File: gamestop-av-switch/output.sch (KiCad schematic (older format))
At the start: 10 parts

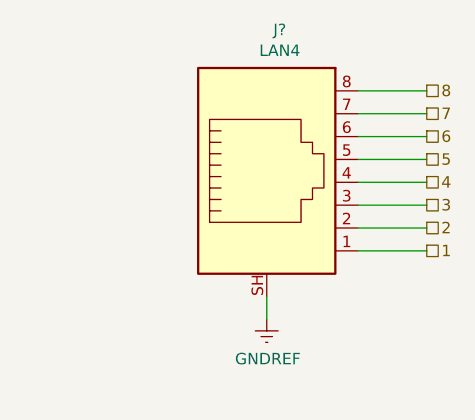
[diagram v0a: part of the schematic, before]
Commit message: Cleaning up extra ethernet pins
Setting no connects on the ports themselves and eliminating the extra
heirarchal labels and pins
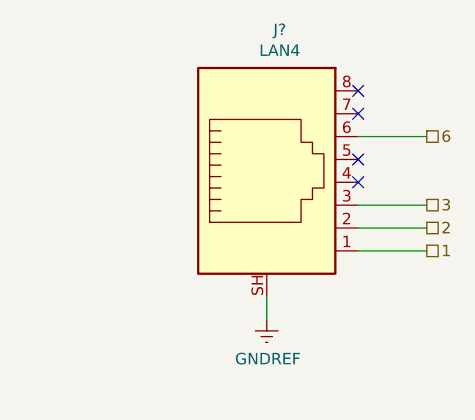
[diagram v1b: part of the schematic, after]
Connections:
- net 4: no longer names the net of J?.4
- net 5: no longer names the net of J?.5
- net 7: no longer names the net of J?.7
- net 8: no longer names the net of J?.8
- no-connect marks 0 -> 4
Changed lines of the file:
@@
 Text HLabel 9850 3600 2    50   UnSpc ~ 0
 3
-Text HLabel 9850 3500 2    50   UnSpc ~ 0
-4
-Text HLabel 9850 3400 2    50   UnSpc ~ 0
-5
 Text HLabel 9850 3300 2    50   UnSpc ~ 0
 6
-Text HLabel 9850 3200 2    50   UnSpc ~ 0
-7
-Text HLabel 9850 3100 2    50   UnSpc ~ 0
-8
-Wire Wire Line
-	9550 3100 9850 3100
-Wire Wire Line
-	9550 3200 9850 3200
 Wire Wire Line
 	9550 3300 9850 3300
-Wire Wire Line
-	9550 3400 9850 3400
-Wire Wire Line
-	9550 3500 9850 3500
 Wire Wire Line
 	9550 3600 9850 3600
@@
 Wire Wire Line
 	2000 3400 2200 3400
+NoConn ~ 9550 3100
+NoConn ~ 9550 3200
+NoConn ~ 9550 3400
+NoConn ~ 9550 3500
 $EndSCHEMATC

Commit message: Annotating and satisfying ERC
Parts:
- gave numbers to parts that had none: 10
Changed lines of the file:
@@
 AR Path="/60F422FE/60FA378A" Ref="J?"  Part="1"
 AR Path="/60F4248B/60FA378A" Ref="J?"  Part="1"
-AR Path="/60F434DB/60FA378A" Ref="J?"  Part="1"
-F 0 "J?" H 4850 3375 50  0000 L CNN
+AR Path="/60F434DB/60FA378A" Ref="J74"  Part="1"
+F 0 "J74" H 4850 3375 50  0000 L CNN
 F 1 "RD5" H 4850 3284 50  0000 L CNN
 F 2 "" H 4750 3400 50  0001 C CNN
@@
 AR Path="/60F422FE/60FA3790" Ref="J?"  Part="1"
 AR Path="/60F4248B/60FA3790" Ref="J?"  Part="1"
-AR Path="/60F434DB/60FA3790" Ref="J?"  Part="1"
-F 0 "J?" H 7150 4017 50  0000 C CNN
+AR Path="/60F434DB/60FA3790" Ref="J76"  Part="1"
+F 0 "J76" H 7150 4017 50  0000 C CNN
 F 1 "SV5" H 7150 3926 50  0000 C CNN
 F 2 "" H 7150 3650 50  0001 C CNN
@@
 AR Path="/60F422FE/60FA3796" Ref="J?"  Part="1"
 AR Path="/60F4248B/60FA3796" Ref="J?"  Part="1"
-AR Path="/60F434DB/60FA3796" Ref="J?"  Part="1"
-F 0 "J?" H 9207 4167 50  0000 C CNN
+AR Path="/60F434DB/60FA3796" Ref="J77"  Part="1"
+F 0 "J77" H 9207 4167 50  0000 C CNN
 F 1 "LAN4" H 9207 4076 50  0000 C CNN
 F 2 "" V 9150 3525 50  0001 C CNN
@@
 AR Path="/60F422FE/60FA379C" Ref="J?"  Part="1"
 AR Path="/60F4248B/60FA379C" Ref="J?"  Part="1"
-AR Path="/60F434DB/60FA379C" Ref="J?"  Part="1"
-F 0 "J?" H 4850 3825 50  0000 L CNN
+AR Path="/60F434DB/60FA379C" Ref="J75"  Part="1"
+F 0 "J75" H 4850 3825 50  0000 L CNN
 F 1 "G5" H 4850 3734 50  0000 L CNN
 F 2 "" H 4750 3850 50  0001 C CNN
@@
 AR Path="/60F422FE/60FA37A2" Ref="J?"  Part="1"
 AR Path="/60F4248B/60FA37A2" Ref="J?"  Part="1"
-AR Path="/60F434DB/60FA37A2" Ref="J?"  Part="1"
-F 0 "J?" H 3600 3375 50  0000 L CNN
+AR Path="/60F434DB/60FA37A2" Ref="J72"  Part="1"
+F 0 "J72" H 3600 3375 50  0000 L CNN
 F 1 "B5" H 3600 3284 50  0000 L CNN
 F 2 "" H 3500 3400 50  0001 C CNN
@@
 AR Path="/60F422FE/60FA37A8" Ref="J?"  Part="1"
 AR Path="/60F4248B/60FA37A8" Ref="J?"  Part="1"
-AR Path="/60F434DB/60FA37A8" Ref="J?"  Part="1"
-F 0 "J?" H 3600 3825 50  0000 L CNN
+AR Path="/60F434DB/60FA37A8" Ref="J73"  Part="1"
+F 0 "J73" H 3600 3825 50  0000 L CNN
 F 1 "Y5" H 3600 3734 50  0000 L CNN
 F 2 "" H 3500 3850 50  0001 C CNN
@@
 AR Path="/60F422FE/60FA37AE" Ref="J?"  Part="1"
 AR Path="/60F4248B/60FA37AE" Ref="J?"  Part="1"
-AR Path="/60F434DB/60FA37AE" Ref="J?"  Part="1"
-F 0 "J?" H 2500 3375 50  0000 L CNN
+AR Path="/60F434DB/60FA37AE" Ref="J70"  Part="1"
+F 0 "J70" H 2500 3375 50  0000 L CNN
 F 1 "R5-2" H 2500 3284 50  0000 L CNN
 F 2 "" H 2400 3400 50  0001 C CNN
@@
 AR Path="/60F422FE/60FA37B4" Ref="J?"  Part="1"
 AR Path="/60F4248B/60FA37B4" Ref="J?"  Part="1"
-AR Path="/60F434DB/60FA37B4" Ref="J?"  Part="1"
-F 0 "J?" H 2500 3825 50  0000 L CNN
+AR Path="/60F434DB/60FA37B4" Ref="J71"  Part="1"
+F 0 "J71" H 2500 3825 50  0000 L CNN
 F 1 "L5-2" H 2500 3734 50  0000 L CNN
 F 2 "" H 2400 3850 50  0001 C CNN
@@
 C
 $Comp
-L power:GNDREF #PWR?
+L power:GNDREF #PWR02
 U 1 1 60FA37C1
 P 5150 4350
-F 0 "#PWR?" H 5150 4100 50  0001 C CNN
+F 0 "#PWR02" H 5150 4100 50  0001 C CNN
 F 1 "GNDREF" H 5155 4177 50  0000 C CNN
 F 2 "" H 5150 4350 50  0001 C CNN
@@
 Connection ~ 7150 4050
 $Comp
-L power:GNDREF #PWR?
+L power:GNDREF #PWR03
 U 1 1 60FA37EB
 P 6750 4200
-F 0 "#PWR?" H 6750 3950 50  0001 C CNN
+F 0 "#PWR03" H 6750 3950 50  0001 C CNN
 F 1 "GNDREF" H 6755 4027 50  0000 C CNN
 F 2 "" H 6750 4200 50  0001 C CNN
@@
 	9550 3800 9850 3800
 $Comp
-L power:GNDREF #PWR?
+L power:GNDREF #PWR04
 U 1 1 60FA3803
 P 9150 4100
-F 0 "#PWR?" H 9150 3850 50  0001 C CNN
+F 0 "#PWR04" H 9150 3850 50  0001 C CNN
 F 1 "GNDREF" H 9155 3927 50  0000 C CNN
 F 2 "" H 9150 4100 50  0001 C CNN
@@
 AR Path="/60F422FE/60FA53D9" Ref="J?"  Part="1"
 AR Path="/60F4248B/60FA53D9" Ref="J?"  Part="1"
-AR Path="/60F434DB/60FA53D9" Ref="J?"  Part="1"
-F 0 "J?" H 1700 3375 50  0000 L CNN
+AR Path="/60F434DB/60FA53D9" Ref="J68"  Part="1"
+F 0 "J68" H 1700 3375 50  0000 L CNN
 F 1 "R5-1" H 1700 3284 50  0000 L CNN
 F 2 "" H 1600 3400 50  0001 C CNN
@@
 AR Path="/60F422FE/60FA53DF" Ref="J?"  Part="1"
 AR Path="/60F4248B/60FA53DF" Ref="J?"  Part="1"
-AR Path="/60F434DB/60FA53DF" Ref="J?"  Part="1"
-F 0 "J?" H 1700 3825 50  0000 L CNN
+AR Path="/60F434DB/60FA53DF" Ref="J69"  Part="1"
+F 0 "J69" H 1700 3825 50  0000 L CNN
 F 1 "L5-1" H 1700 3734 50  0000 L CNN
 F 2 "" H 1600 3850 50  0001 C CNN
